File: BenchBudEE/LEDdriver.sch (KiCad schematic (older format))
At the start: 0 parts

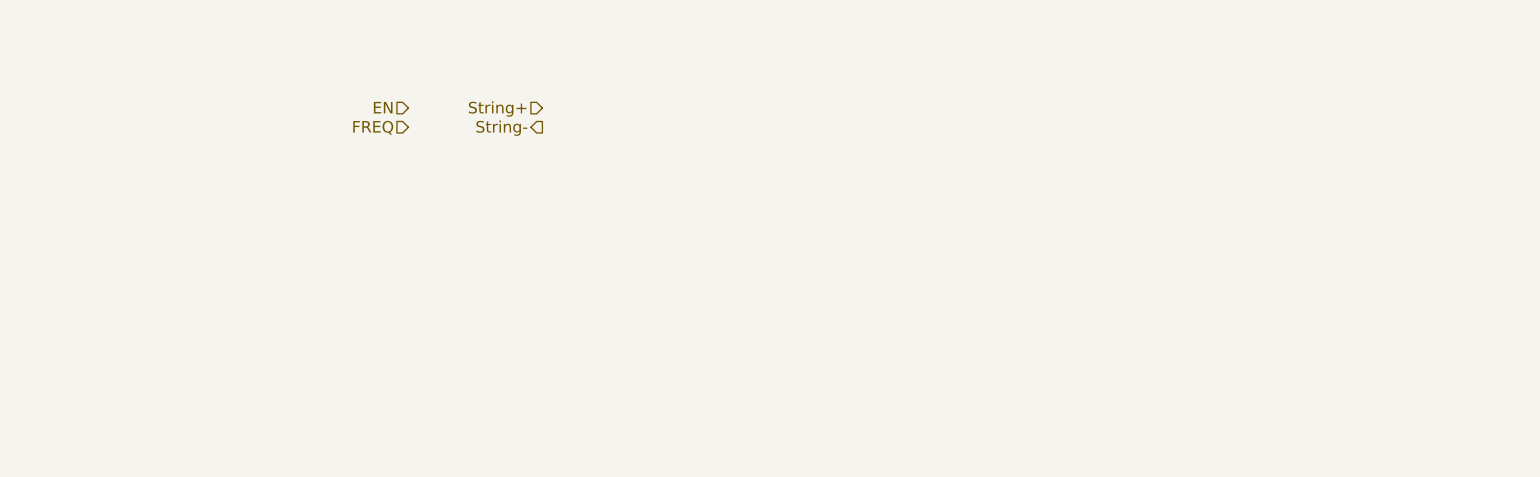
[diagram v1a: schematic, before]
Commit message: Completing schematics from week 3 videos.
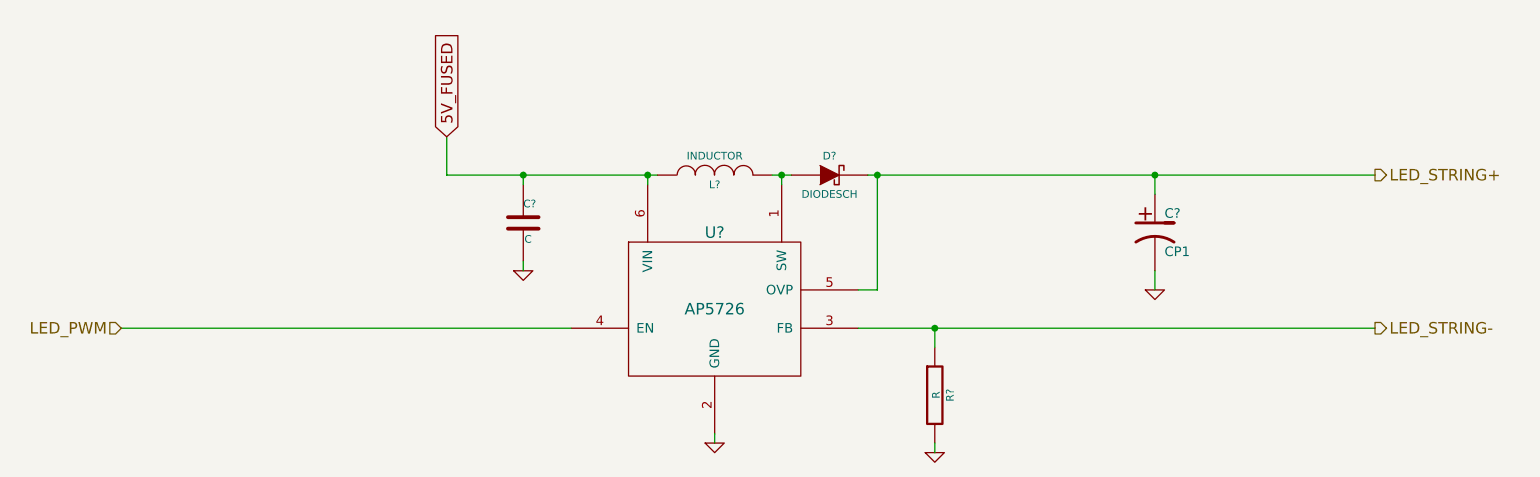
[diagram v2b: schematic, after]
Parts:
- added C?: C, ~, symbol C
- added C?: CP1, ~, symbol CP1
- added D?: DIODESCH, ~, symbol DIODESCH
- added L?: INDUCTOR, ~, symbol INDUCTOR
- added R?: R, ~, symbol R
- added U?: AP5726, ~, symbol AP5726
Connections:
- new net: D?.1 (A), L?.2, U?.1 (SW)
- new net 5V_FUSED: C?.1, L?.1, U?.6 (VIN)
- new net GND: C?.2, C?.2, R?.2, U?.2 (GND)
- new net LED_PWM: U?.4 (EN)
- new net LED_STRING+: C?.1, D?.2 (K), U?.5 (OVP)
- new net LED_STRING-: R?.1, U?.3 (FB)
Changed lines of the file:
@@
 LIBS:relay_spdt
 LIBS:5566-20A
+LIBS:AP5726
+LIBS:arduino
 LIBS:BenchBudEE-cache
 EELAYER 27 0
@@
 $Descr A4 11693 8268
 encoding utf-8
-Sheet 6 9
+Sheet 5 9
 Title ""
-Date "13 feb 2014"
+Date "24 feb 2014"
 Rev ""
 Comp ""
@@
 Comment4 ""
 $EndDescr
-Text HLabel 4050 2900 0    60   Input ~ 0
-EN
-Text HLabel 4050 3000 0    60   Input ~ 0
-FREQ
-Text HLabel 4750 2900 0    60   Input ~ 0
-String+
-Text HLabel 4750 3000 0    60   Output ~ 0
-String-
+Text HLabel 2550 4050 0    60   Input ~ 0
+LED_PWM
+Text HLabel 9100 3250 2    60   Output ~ 0
+LED_STRING+
+Text HLabel 9100 4050 2    60   Output ~ 0
+LED_STRING-
+$Comp
+L AP5726 U?
+U 1 1 530A5517
+P 5650 3950
+F 0 "U?" H 5650 4350 60  0000 C CNN
+F 1 "AP5726" H 5650 3950 60  0000 C CNN
+F 2 "~" H 5650 3950 60  0000 C CNN
+F 3 "~" H 5650 3950 60  0000 C CNN
+	1    5650 3950
+	1    0    0    -1
+$EndComp
+$Comp
+L INDUCTOR L?
+U 1 1 530A5526
+P 5650 3250
+F 0 "L?" V 5600 3250 40  0000 C CNN
+F 1 "INDUCTOR" V 5750 3250 40  0000 C CNN
+F 2 "~" H 5650 3250 60  0000 C CNN
+F 3 "~" H 5650 3250 60  0000 C CNN
+	1    5650 3250
+	0    -1   -1   0
+$EndComp
+Wire Wire Line
+	5950 3250 6050 3250
+Wire Wire Line
+	6000 3300 6000 3250
+Connection ~ 6000 3250
+$Comp
+L C C?
+U 1 1 530A5573
+P 4650 3500
+F 0 "C?" H 4650 3600 40  0000 L CNN
+F 1 "C" H 4656 3415 40  0000 L CNN
+F 2 "~" H 4688 3350 30  0000 C CNN
+F 3 "~" H 4650 3500 60  0000 C CNN
+	1    4650 3500
+	1    0    0    -1
+$EndComp
+$Comp
+L GND #PWR?
+U 1 1 530A5582
+P 4650 3750
+F 0 "#PWR?" H 4650 3750 30  0001 C CNN
+F 1 "GND" H 4650 3680 30  0001 C CNN
+F 2 "" H 4650 3750 60  0000 C CNN
+F 3 "" H 4650 3750 60  0000 C CNN
+	1    4650 3750
+	1    0    0    -1
+$EndComp
+Wire Wire Line
+	4650 3700 4650 3750
+Wire Wire Line
+	5350 3250 4250 3250
+Wire Wire Line
+	4250 3250 4250 3050
+Wire Wire Line
+	4650 3300 4650 3250
+Connection ~ 4650 3250
+Wire Wire Line
+	5300 3300 5300 3250
+Connection ~ 5300 3250
+$Comp
+L GND #PWR?
+U 1 1 530A55CB
+P 5650 4650
+F 0 "#PWR?" H 5650 4650 30  0001 C CNN
+F 1 "GND" H 5650 4580 30  0001 C CNN
+F 2 "" H 5650 4650 60  0000 C CNN
+F 3 "" H 5650 4650 60  0000 C CNN
+	1    5650 4650
+	1    0    0    -1
+$EndComp
+Wire Wire Line
+	5650 4600 5650 4650
+$Comp
+L R R?
+U 1 1 530A55EA
+P 6800 4400
+F 0 "R?" V 6880 4400 40  0000 C CNN
+F 1 "R" V 6807 4401 40  0000 C CNN
+F 2 "~" V 6730 4400 30  0000 C CNN
+F 3 "~" H 6800 4400 30  0000 C CNN
+	1    6800 4400
+	1    0    0    -1
+$EndComp
+Wire Wire Line
+	6400 4050 9100 4050
+$Comp
+L GND #PWR?
+U 1 1 530A5605
+P 6800 4700
+F 0 "#PWR?" H 6800 4700 30  0001 C CNN
+F 1 "GND" H 6800 4630 30  0001 C CNN
+F 2 "" H 6800 4700 60  0000 C CNN
+F 3 "" H 6800 4700 60  0000 C CNN
+	1    6800 4700
+	1    0    0    -1
+$EndComp
+Text GLabel 4250 3050 1    60   Input ~ 0
+5V_FUSED
+Wire Wire Line
+	6400 3850 6500 3850
+Wire Wire Line
+	6500 3850 6500 3250
+Wire Wire Line
+	6450 3250 9100 3250
+$Comp
+L DIODESCH D?
+U 1 1 530A5676
+P 6250 3250
+F 0 "D?" H 6250 3350 40  0000 C CNN
+F 1 "DIODESCH" H 6250 3150 40  0000 C CNN
+F 2 "~" H 6250 3250 60  0000 C CNN
+F 3 "~" H 6250 3250 60  0000 C CNN
+	1    6250 3250
+	1    0    0    -1
+$EndComp
+Wire Wire Line
+	6800 4650 6800 4700
+Connection ~ 6800 4050
+$Comp
+L CP1 C?
+U 1 1 530A5703
+P 7950 3550
+F 0 "C?" H 8000 3650 50  0000 L CNN
+F 1 "CP1" H 8000 3450 50  0000 L CNN
+F 2 "~" H 7950 3550 60  0000 C CNN
+F 3 "~" H 7950 3550 60  0000 C CNN
+	1    7950 3550
+	1    0    0    -1
+$EndComp
+$Comp
+L GND #PWR?
+U 1 1 530A5712
+P 7950 3850
+F 0 "#PWR?" H 7950 3850 30  0001 C CNN
+F 1 "GND" H 7950 3780 30  0001 C CNN
+F 2 "" H 7950 3850 60  0000 C CNN
+F 3 "" H 7950 3850 60  0000 C CNN
+	1    7950 3850
+	1    0    0    -1
+$EndComp
+Wire Wire Line
+	7950 3750 7950 3850
+Wire Wire Line
+	7950 3250 7950 3350
+Connection ~ 6500 3250
+Connection ~ 7950 3250
+Wire Wire Line
+	6800 4050 6800 4150
+Wire Wire Line
+	4900 4050 2550 4050
 $EndSCHEMATC

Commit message: checking in all my local changes before syncing to chris's repo.
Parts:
- gave numbers to parts that had none: 6
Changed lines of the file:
@@
 Sheet 5 9
 Title ""
-Date "24 feb 2014"
+Date "2 mar 2014"
 Rev ""
 Comp ""
@@
 LED_STRING-
 $Comp
-L AP5726 U?
+L AP5726 U5
 U 1 1 530A5517
 P 5650 3950
-F 0 "U?" H 5650 4350 60  0000 C CNN
+F 0 "U5" H 5650 4350 60  0000 C CNN
 F 1 "AP5726" H 5650 3950 60  0000 C CNN
 F 2 "~" H 5650 3950 60  0000 C CNN
@@
 $EndComp
 $Comp
-L INDUCTOR L?
+L INDUCTOR L3
 U 1 1 530A5526
 P 5650 3250
-F 0 "L?" V 5600 3250 40  0000 C CNN
+F 0 "L3" V 5600 3250 40  0000 C CNN
 F 1 "INDUCTOR" V 5750 3250 40  0000 C CNN
 F 2 "~" H 5650 3250 60  0000 C CNN
@@
 Connection ~ 6000 3250
 $Comp
-L C C?
+L C C4
 U 1 1 530A5573
 P 4650 3500
-F 0 "C?" H 4650 3600 40  0000 L CNN
+F 0 "C4" H 4650 3600 40  0000 L CNN
 F 1 "C" H 4656 3415 40  0000 L CNN
 F 2 "~" H 4688 3350 30  0000 C CNN
@@
 $EndComp
 $Comp
-L GND #PWR?
+L GND #PWR20
 U 1 1 530A5582
 P 4650 3750
-F 0 "#PWR?" H 4650 3750 30  0001 C CNN
+F 0 "#PWR20" H 4650 3750 30  0001 C CNN
 F 1 "GND" H 4650 3680 30  0001 C CNN
 F 2 "" H 4650 3750 60  0000 C CNN
@@
 Connection ~ 5300 3250
 $Comp
-L GND #PWR?
+L GND #PWR21
 U 1 1 530A55CB
 P 5650 4650
-F 0 "#PWR?" H 5650 4650 30  0001 C CNN
+F 0 "#PWR21" H 5650 4650 30  0001 C CNN
 F 1 "GND" H 5650 4580 30  0001 C CNN
 F 2 "" H 5650 4650 60  0000 C CNN
@@
 	5650 4600 5650 4650
 $Comp
-L R R?
+L R R16
 U 1 1 530A55EA
 P 6800 4400
-F 0 "R?" V 6880 4400 40  0000 C CNN
+F 0 "R16" V 6880 4400 40  0000 C CNN
 F 1 "R" V 6807 4401 40  0000 C CNN
 F 2 "~" V 6730 4400 30  0000 C CNN
@@
 	6400 4050 9100 4050
 $Comp
-L GND #PWR?
+L GND #PWR22
 U 1 1 530A5605
 P 6800 4700
-F 0 "#PWR?" H 6800 4700 30  0001 C CNN
+F 0 "#PWR22" H 6800 4700 30  0001 C CNN
 F 1 "GND" H 6800 4630 30  0001 C CNN
 F 2 "" H 6800 4700 60  0000 C CNN
@@
 	6450 3250 9100 3250
 $Comp
-L DIODESCH D?
+L DIODESCH D4
 U 1 1 530A5676
 P 6250 3250
-F 0 "D?" H 6250 3350 40  0000 C CNN
+F 0 "D4" H 6250 3350 40  0000 C CNN
 F 1 "DIODESCH" H 6250 3150 40  0000 C CNN
 F 2 "~" H 6250 3250 60  0000 C CNN
@@
 Connection ~ 6800 4050
 $Comp
-L CP1 C?
+L CP1 C5
 U 1 1 530A5703
 P 7950 3550
-F 0 "C?" H 8000 3650 50  0000 L CNN
+F 0 "C5" H 8000 3650 50  0000 L CNN
 F 1 "CP1" H 8000 3450 50  0000 L CNN
 F 2 "~" H 7950 3550 60  0000 C CNN
@@
 $EndComp
 $Comp
-L GND #PWR?
+L GND #PWR23
 U 1 1 530A5712
 P 7950 3850
-F 0 "#PWR?" H 7950 3850 30  0001 C CNN
+F 0 "#PWR23" H 7950 3850 30  0001 C CNN
 F 1 "GND" H 7950 3780 30  0001 C CNN
 F 2 "" H 7950 3850 60  0000 C CNN
